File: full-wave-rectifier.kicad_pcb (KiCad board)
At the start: 2 copper layers, 80.6 x 108 mm, 64 parts, among them J10 Control Right, J11 Main Right, J12 Power Connector, J2 Input Ch1, J3 Input Ch2, J4 Output Ch1, J5 Output Ch2, J6 Ochd input, J8 Control Left, J9 Main Left, Q7 AO3404A, Q8 AO3407A, U1 LM78L05_TO92, U2 TL074, U3 TL074, U4 TL074

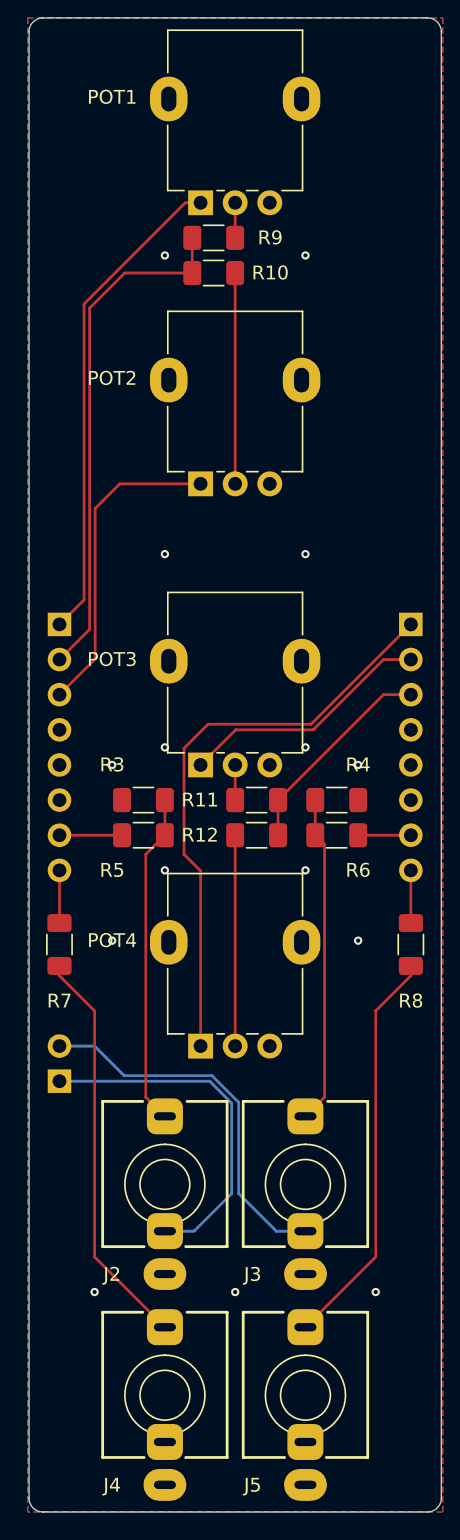
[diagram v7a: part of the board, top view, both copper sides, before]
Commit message: updated footprints
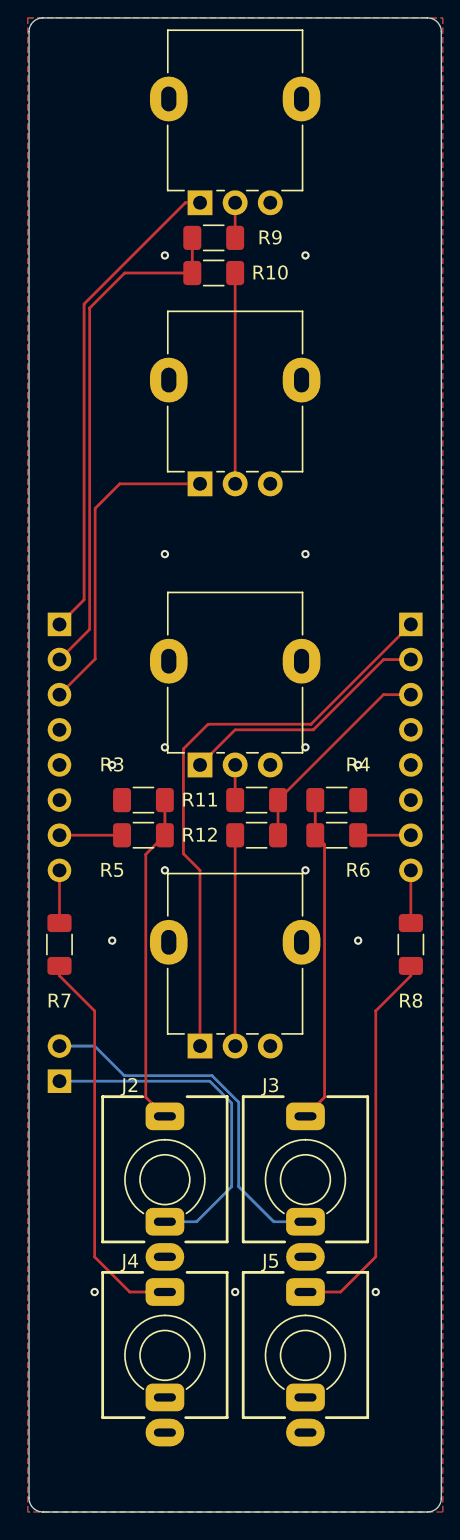
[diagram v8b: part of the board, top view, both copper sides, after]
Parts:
- removed POT1: 9mm_NoDet_10k_DShaft, Potentiometer_THT:Potentiometer_Alpha_RD901F-40-00D_Single_Vertical
- added AMP_CH1: 10k, Eurorack:Pot_Alpha_9mm, F.Cu at (127.0, 61.0)
- AMP_CH2: renamed from POT3; value 9mm_NoDet_10k_DShaft -> 10k; footprint Potentiometer_THT:Potentiometer_Alpha_RD901F-40-00D_Single_Vertical -> Eurorack:Pot_Alpha_9mm
- J2, J3, J4, J5: footprint AudioJacks:Jack_3.5mm_QingPu_WQP-PJ398SM_Vertical -> Eurorack:Jack_3.5mm_WQP518MA
- OFFSET_CH1: renamed from POT2; value 9mm_NoDet_10k_DShaft -> 10k; footprint Potentiometer_THT:Potentiometer_Alpha_RD901F-40-00D_Single_Vertical -> Eurorack:Pot_Alpha_9mm
- OFFSET_CH2: renamed from POT4; value 9mm_NoDet_10k_DShaft -> 10k; footprint Potentiometer_THT:Potentiometer_Alpha_RD901F-40-00D_Single_Vertical -> Eurorack:Pot_Alpha_9mm
- moved J2 2.70 mm to (121.9, 134.6)
- moved J3 2.70 mm to (132.1, 134.6)
- moved AMP_CH2 2.50 mm to (127.0, 101.6), turned to 0 degrees
- moved OFFSET_CH1 2.50 mm to (127.0, 81.3), turned to 0 degrees
- moved OFFSET_CH2 2.50 mm to (127.0, 121.9), turned to 0 degrees
- moved J4 0.16 mm to (121.9, 147.3)
- moved J5 0.16 mm to (132.1, 147.3)
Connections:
- AMP_CH2 pad : GND -> (no net)
- OFFSET_CH1 pad : GND -> (no net)
- OFFSET_CH2 pad : GND -> (no net)
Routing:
- net Net-(J5-PadT): track 29.3 -> 28.2 mm
- net Net-(J4-PadT): track 29.3 -> 28.2 mm
- net OCHD_CH2: track 27.2 -> 26.6 mm
- net OCHD_CH1: track 25.6 -> 25.0 mm
